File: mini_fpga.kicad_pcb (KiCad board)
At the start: 2 copper layers, 50.8 x 25.4 mm, 0 parts

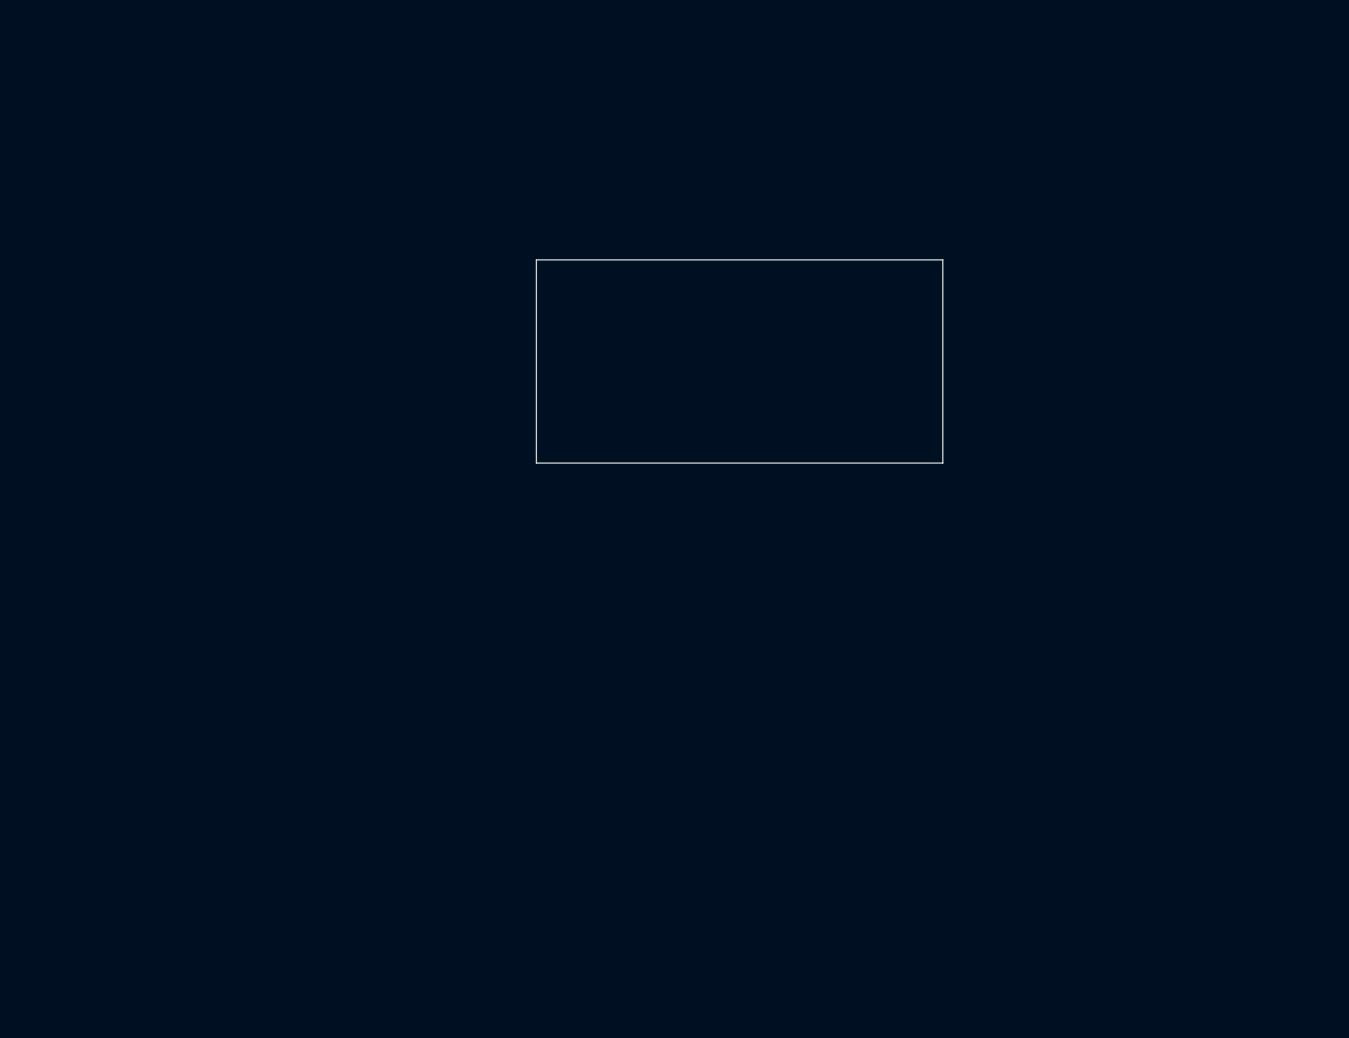
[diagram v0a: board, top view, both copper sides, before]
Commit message: Final state of 2sqin design, going to move to 4sqin to actually be able to complete the design.
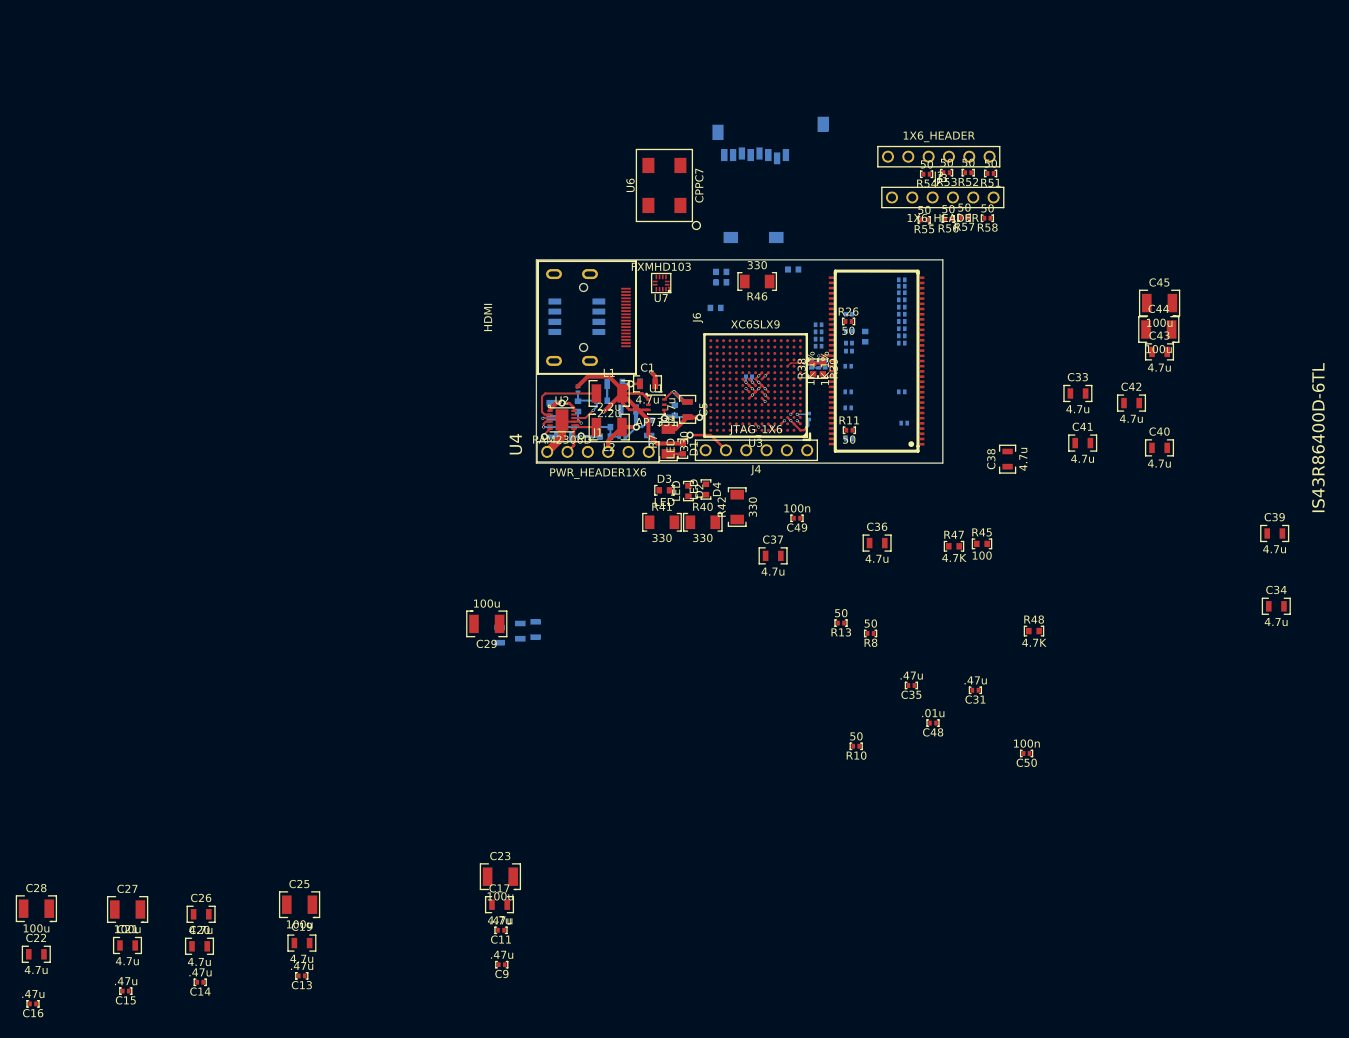
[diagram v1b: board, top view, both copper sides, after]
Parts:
- added C1: 4.7u, 0805_custom, F.Cu at (166.3, 142.5)
- added C10: .47u, 0402_murata, B.Cu at (179.0, 141.6)
- added C11: .47u, 0402_murata, F.Cu at (148.0, 210.8)
- added C12: 4.7u, 0805_custom, B.Cu at (152.3, 173.2)
- added C13: .47u, 0402_murata, F.Cu at (123.1, 216.5)
- added C14: .47u, 0402_murata, F.Cu at (110.4, 217.3)
- added C15: .47u, 0402_murata, F.Cu at (101.1, 218.4)
- added C16: .47u, 0402_murata, F.Cu at (89.5, 220.0)
- added C17: 4.7u, 0805_custom, F.Cu at (147.8, 207.6)
- added C18: 4.7u, 0805_custom, B.Cu at (150.4, 173.4)
- added C19: 4.7u, 0805_custom, F.Cu at (123.1, 212.4)
- added C2: 4.7u, 0805_custom, B.Cu at (154.3, 145.8)
- added C20: 4.7u, 0805_custom, F.Cu at (110.3, 212.8)
- added C21: 4.7u, 0805_custom, F.Cu at (101.3, 212.7)
- added C22: 4.7u, 0805_custom, F.Cu at (89.9, 213.8)
- added C23: 100u, 1210_murata, F.Cu at (147.9, 204.1)
- added C24: 4.7u, 0805_custom, B.Cu at (147.8, 173.9)
- added C25: 100u, 1210_murata, F.Cu at (122.8, 207.6)
- added C26: 4.7u, 0805_custom, F.Cu at (110.5, 208.8)
- added C27: 100u, 1210_murata, F.Cu at (101.3, 208.2)
- added C28: 100u, 1210_murata, F.Cu at (89.9, 208.1)
- added C29: 100u, 1210_murata, F.Cu at (146.2, 172.5)
- added C3: 10u, 0805_custom, B.Cu at (166.5, 148.0)
- added C30: .1u, 0402_murata, B.Cu at (186.8, 140.1)
- added C31: .47u, 0402_murata, F.Cu at (207.3, 180.8)
- added C32: .1u, 0402_murata, B.Cu at (186.4, 146.6)
- added C33: 4.7u, 0805_custom, F.Cu at (220.1, 143.7)
- added C34: 4.7u, 0805_custom, F.Cu at (244.9, 170.3)
- added C35: .47u, 0402_murata, F.Cu at (199.3, 180.2)
- added C36: 4.7u, 0805_custom, F.Cu at (195.0, 162.4)
- added C37: 4.7u, 0805_custom, F.Cu at (182.0, 164.0)
- added C38: 4.7u, 0805_custom, F.Cu at (211.3, 151.9)
- added C39: 4.7u, 0805_custom, F.Cu at (244.7, 161.2)
- added C4: 100p, 0402_murata, B.Cu at (163.1, 149.1)
- added C40: 4.7u, 0805_custom, F.Cu at (230.3, 150.5)
- added C41: 4.7u, 0805_custom, F.Cu at (220.7, 149.9)
- added C42: 4.7u, 0805_custom, F.Cu at (226.8, 144.9)
- added C43: 4.7u, 0805_custom, F.Cu at (230.3, 138.5)
- added C44: 100u, 1210_murata, F.Cu at (230.2, 135.7)
- added C45: 100u, 1210_murata, F.Cu at (230.3, 132.4)
- added C46: .1u, 0402_murata, B.Cu at (188.5, 140.1)
- added C47: .1u, 0402_murata, B.Cu at (187.7, 140.2)
- added C48: .01u, 0402_murata, F.Cu at (202.0, 184.9)
- added C49: 100n, 0402_murata, F.Cu at (185.0, 159.3)
- added C5: 4.7u, 0805_custom, F.Cu at (171.3, 145.7)
- added C50: 100n, 0402_murata, F.Cu at (213.7, 188.7)
- added C6: 100p, 0402_murata, B.Cu at (157.6, 143.2)
- added C7: 10u, 0805_custom, B.Cu at (166.3, 142.5)
- added C8: 4.7u, 0805_custom, B.Cu at (155.9, 149.1)
- added C9: .47u, 0402_murata, F.Cu at (148.1, 215.1)
- added D1: LED, 0603_custom, F.Cu at (170.7, 150.6)
- added D2: LED, 0603_custom, F.Cu at (171.4, 155.9)
- added D3: LED, 0603_custom, F.Cu at (168.4, 155.8)
- added D4: LED, 0603_custom, F.Cu at (173.6, 155.7)
- added J1: PWR_HEADER1X6, header_1x6, F.Cu at (160.1, 151.0)
- added J2: 1X6_HEADER, header_1x6, F.Cu at (202.7, 114.1)
- added J3: 1X6_HEADER, header_1x6, F.Cu at (203.2, 119.2)
- added J4: JTAG_1X6, header_1x6, F.Cu at (179.9, 150.8)
- added J5: USD_SLOT, uSD_slot, B.Cu at (180.0, 114.9)
- added J6: HDMI, mini_HDMI, F.Cu at (160.5, 134.2)
- added L1: 2.2u, 1210_murata, F.Cu at (161.5, 143.7)
- added L2: 2.2u, 1210_murata, F.Cu at (161.5, 147.9)
- added R1: 340k1%, 0805_custom, B.Cu at (163.9, 145.7)
- added R10: 50, 0402_murata, F.Cu at (192.4, 187.8)
- added R11: 50, 0402_murata, F.Cu at (191.5, 148.3)
- added R12: 50, 0402_murata, B.Cu at (191.5, 137.4)
- added R13: 50, 0402_murata, F.Cu at (190.5, 172.4)
- added R14: 50, 0402_murata, B.Cu at (187.7, 136.0)
- added R15: 50, 0402_murata, B.Cu at (191.5, 149.4)
- added R16: 50, 0402_murata, B.Cu at (198.4, 147.4)
- added R17: 50, 0402_murata, B.Cu at (191.4, 140.3)
- added R18: 50, 0402_murata, B.Cu at (191.4, 143.5)
- added R19: 50, 0402_murata, B.Cu at (191.4, 145.5)
- added R2: 120k1%, 0603_custom, B.Cu at (161.0, 149.1)
- added R20: 50, 0402_murata, B.Cu at (198.1, 135.6)
- added R21: 50, 0402_murata, B.Cu at (198.1, 136.5)
- added R22: 50, 0402_murata, B.Cu at (198.1, 129.5)
- added R23: 50, 0402_murata, B.Cu at (198.1, 132.9)
- added R24: 50, 0402_murata, B.Cu at (187.7, 135.1)
- added R25: 50, 0402_murata, B.Cu at (191.5, 135.9)
- added R26: 50, 0402_murata, F.Cu at (191.4, 134.7)
- added R27: 50, 0402_murata, B.Cu at (198.1, 132.0)
- added R28: 50, 0402_murata, B.Cu at (198.1, 131.1)
- added R29: 50, 0402_murata, B.Cu at (187.7, 136.9)
- added R3: 200k1%, 0805_custom, B.Cu at (171.3, 145.7)
- added R30: 50, 0402_murata, B.Cu at (198.1, 130.3)
- added R31: 100, 0603_custom, B.Cu at (193.5, 136.6)
- added R32: 50, 0402_murata, B.Cu at (187.7, 137.8)
- added R33: 50, 0402_murata, B.Cu at (191.5, 138.4)
- added R34: 50, 0402_murata, B.Cu at (191.5, 133.8)
- added R35: 50, 0402_murata, B.Cu at (198.1, 134.7)
- added R36: 50, 0402_murata, B.Cu at (198.1, 133.8)
- added R37: 50, 0402_murata, B.Cu at (198.1, 137.4)
- added R38: 1K 1%, 0603_custom, F.Cu at (187.0, 140.6)
- added R39: 1K 1%, 0603_custom, F.Cu at (188.2, 140.6)
- added R4: 100k1%, 0603_custom, B.Cu at (169.7, 145.8)
- added R40: 330, 1206_custom, F.Cu at (173.2, 159.8)
- added R41: 330, 1206_custom, F.Cu at (168.1, 159.8)
- added R42: 330, 1206_custom, F.Cu at (177.5, 157.9)
- added R43: 100, 0603_custom, B.Cu at (175.5, 129.8)
- added R44: 100, 0603_custom, B.Cu at (175.5, 128.5)
- added R45: 100, 0603_custom, F.Cu at (208.1, 162.5)
- added R46: 330, 1206_custom, F.Cu at (180.0, 129.7)
- added R47: 4.7K, 0603_custom, F.Cu at (204.6, 162.8)
- added R48: 4.7K, 0603_custom, F.Cu at (214.6, 173.4)
- added R49: 4.7K, 0603_custom, B.Cu at (184.5, 128.2)
- added R5: 510k .5%, 0805_custom, B.Cu at (162.2, 142.5)
- added R50: 4.7K, 0603_custom, B.Cu at (174.8, 133.0)
- added R51: 50, 0402_murata, F.Cu at (209.2, 116.2)
- added R52: 50, 0402_murata, F.Cu at (206.4, 116.1)
- added R53: 50, 0402_murata, F.Cu at (203.7, 116.1)
- added R54: 50, 0402_murata, F.Cu at (201.2, 116.3)
- added R55: 50, 0402_murata, F.Cu at (200.9, 122.0)
- added R56: 50, 0402_murata, F.Cu at (203.9, 121.9)
- added R57: 50, 0402_murata, F.Cu at (205.9, 121.7)
- added R58: 50, 0402_murata, F.Cu at (208.8, 121.8)
- added R59: 30k .5%, 0603_custom, B.Cu at (160.6, 144.6)
- added R6: 120k1%, 0603_custom, B.Cu at (157.6, 145.3)
- added R60: 40k1%, 0603_custom, B.Cu at (162.3, 147.9)
- added R7: 330, 1206_custom, F.Cu at (168.9, 149.7)
- added R8: 50, 0402_murata, F.Cu at (194.2, 173.7)
- added R9: 50, 0402_murata, B.Cu at (198.1, 143.5)
- added U1: AP7331, DFN2020, F.Cu at (167.4, 145.1)
- added U2: PAM2306D, WDFN12, F.Cu at (155.6, 147.0)
- added U3: XC6SLX9, CSG_225_custom, F.Cu at (179.8, 142.7)
- added U4: IS43R86400D-6TL, TSOP66, F.Cu at (200.9, 150.2)
- added U5: S25FL164, SOC8, B.Cu at (157.5, 134.1)
- added U6: CPPC7, CPPC7_SMD, F.Cu at (168.4, 117.7)
- added U7: FXMHD103, UMLP-12, F.Cu at (168.0, 129.9)
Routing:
- net +3.3V: track 0.00 -> 55.3 mm, vias 0 -> 7
- net GND: track 0.00 -> 37.4 mm, vias 0 -> 12
- net +1.2V: track 0.00 -> 27.7 mm, vias 0 -> 8
- net +5V: track 0.00 -> 20.1 mm, vias 0 -> 2
- net /memory/Vref: track 0.00 -> 18.6 mm, vias 0 -> 3
- net N-000008: track 0.00 -> 12.0 mm, vias 0 -> 1
- net +2.5V: track 0.00 -> 11.9 mm, vias 0 -> 2
- net N-000002: track 0.00 -> 10.0 mm
- net N-000001: track 0.00 -> 7.66 mm, vias 0 -> 1
- net N-000005: track 0.00 -> 4.18 mm, vias 0 -> 1
- net N-000003: track 0.00 -> 2.89 mm
- net N-0000014: track 0.00 -> 2.10 mm
- net N-000009: track 0.00 -> 1.80 mm
- net N-000004: track 0.00 -> 1.80 mm
- net (no net): track 0.00 -> 0.57 mm
- added copper zone on InnerB.Cu, net GND
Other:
- copper layers 2 -> 4
- net class Default: clearance 0.254 -> 0.127; trace_width 0.254 -> 0.127
- rule trace_clearance: 0.254 -> 0.127
- rule trace_min: 0.254 -> 0.127
- rule via_min_drill: 0.508 -> 0.254
- rule via_min_size: 0.889 -> 0.3556

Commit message: Capacitor value error correction.
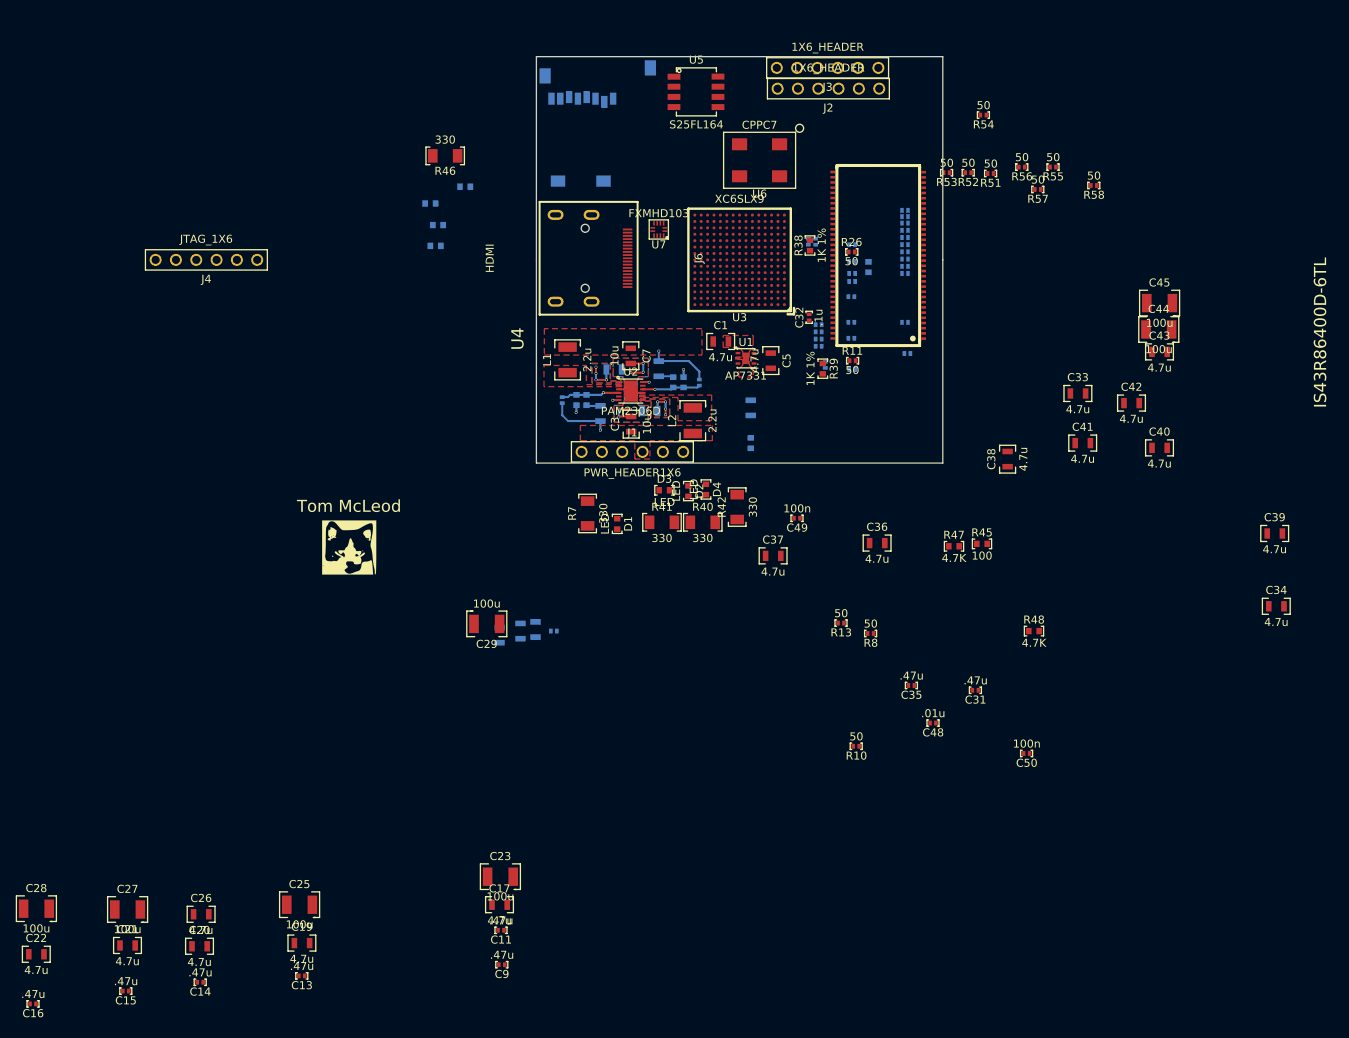
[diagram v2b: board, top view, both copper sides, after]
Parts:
- added G***: LOGO, LOGO, F.Cu at (129.0, 162.9)
- C3, C32, C7, U5: moved to F.Cu
- moved J4 72.8 mm to (111.2, 127.0)
- moved R49 44.8 mm to (139.8, 125.2)
- moved R46 42.0 mm to (141.0, 114.0)
- moved C10 40.1 mm to (154.6, 173.4)
- moved R43 37.7 mm to (139.2, 120.0)
- moved R50 36.2 mm to (140.1, 122.7)
- moved R44 33.7 mm to (143.5, 117.8)
- moved U5 31.8 mm to (172.4, 106.0)
- moved J5 22.7 mm to (158.4, 107.8)
- moved J3 21.7 mm to (188.8, 103.0), turned to 180 degrees
- moved R55 17.4 mm to (217.0, 115.4)
- moved J2 16.2 mm to (188.9, 105.6)
- moved U3 15.8 mm to (177.8, 127.0)
- moved C47 15.4 mm to (187.3, 124.8)
- moved C30 15.4 mm to (186.4, 124.7)
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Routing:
- net +3.3V: track 55.3 -> 7.86 mm, vias 7 -> 1
- net +1.2V: track 27.7 -> 0.00 mm, vias 8 -> 0
- net GND: track 37.4 -> 13.3 mm, vias 12 -> 8
- net /memory/Vref: track 18.6 -> 0.00 mm, vias 3 -> 0
- net +5V: track 20.1 -> 9.52 mm, vias 2 -> 10
- net N-000002: track 10.0 -> 0.00 mm
- net N-000008: track 12.0 -> 7.31 mm
- net N-000005: track 4.18 -> 0.00 mm, vias 1 -> 0
- net +2.5V: track 11.9 -> 7.74 mm, vias 2 -> 1
- net N-000003: track 2.89 -> 0.00 mm
- net N-000004: track 1.80 -> 0.00 mm
- net (no net): track 0.57 -> 0.00 mm
- added copper zone on F.Cu, net +2.5V
- added copper zone on F.Cu, net +3.3V
- added copper zone on B.Cu, net +5V
- added copper zone on F.Cu, net +5V
- added copper zone on InnerF.Cu, net +5V
- added copper zone on B.Cu, net GND
- added copper zone on F.Cu, net GND
- added copper zone on F.Cu, net N-000002
- added copper zone on F.Cu, net N-000003
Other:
- board size 50.8 x 25.4 mm -> 50.8 x 50.8 mm
- board text added: "Tom McLeod"

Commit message: Fixed issue with vias being too small.
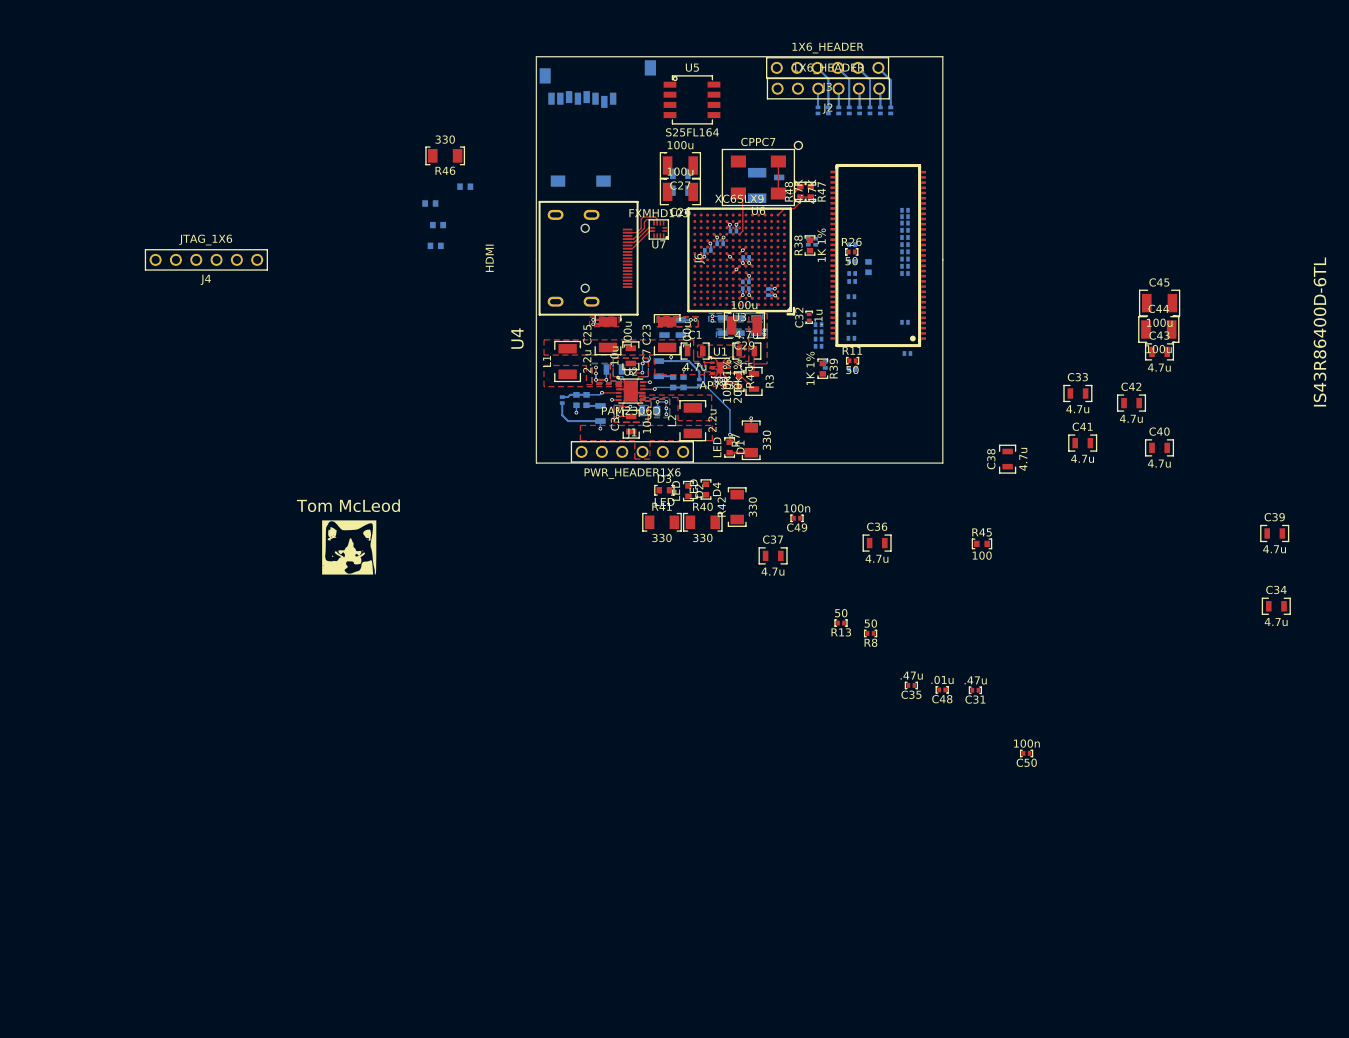
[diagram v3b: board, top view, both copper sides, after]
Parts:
- C11, C13, C14, C15, C16, C17, C19, C20, C21, C22, C28, C9, R10, R51, R52, R53, R54, R55, R56, R57, R58: moved to B.Cu
- C26: value 4.7u -> 100u; footprint 0805_custom -> 1210_murata
- R3, R4: moved to F.Cu
- moved C22 133.7 mm to (182.8, 117.7), turned to 90 degrees
- moved C16 127.9 mm to (181.4, 131.1), turned to 270 degrees
- moved C28 127.6 mm to (180.0, 117.7), turned to 90 degrees
- moved C15 121.6 mm to (177.0, 123.4), turned to 180 degrees
- moved C21 118.6 mm to (170.4, 116.2), turned to 180 degrees
- moved C27 115.9 mm to (170.4, 115.2), turned to 180 degrees
- moved C20 112.0 mm to (170.4, 118.3), turned to 180 degrees
- moved C14 111.3 mm to (173.8, 125.8)
- moved C26 108.4 mm to (170.4, 118.5), turned to 180 degrees
- moved C13 102.3 mm to (178.6, 130.6)
- moved C9 90.6 mm to (178.6, 129.8), turned to 180 degrees
- moved C11 90.1 mm to (175.4, 125.0)
- moved C19 89.3 mm to (168.4, 135.4), turned to 90 degrees
- moved C25 81.0 mm to (161.3, 136.3), turned to 90 degrees
- moved C17 75.6 mm to (170.4, 135.4), turned to 90 degrees
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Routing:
- net GND: track 13.3 -> 44.7 mm, vias 8 -> 27
- net +3.3V: track 7.86 -> 33.5 mm, vias 1 -> 8
- net +1.2V: track 0.00 -> 12.2 mm, vias 0 -> 6
- net N-00000208: track 0.00 -> 5.81 mm
- net N-00000128: track 0.00 -> 5.59 mm
- net N-00000125: track 0.00 -> 5.57 mm
- net N-00000126: track 0.00 -> 5.54 mm
- net N-00000129: track 0.00 -> 5.52 mm
- net N-00000164: track 0.00 -> 5.49 mm
- net N-00000200: track 0.00 -> 5.41 mm
- net N-00000231: track 0.00 -> 5.18 mm
- net N-00000211: track 0.00 -> 4.06 mm
- net N-000005: track 0.00 -> 4.03 mm
- net N-00000232: track 0.00 -> 3.90 mm
- net N-000004: track 0.00 -> 2.70 mm
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- added copper zone on B.Cu, net +1.2V
- added copper zone on F.Cu, net +1.2V
- added copper zone on InnerF.Cu, net +1.2V
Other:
- rule via_min_size: 0.3556 -> 0.4572
